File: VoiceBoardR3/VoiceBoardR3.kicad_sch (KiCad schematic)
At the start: 11 parts, among them U103 VoiceBoardConn_18P_254P, U302 TMUX4053

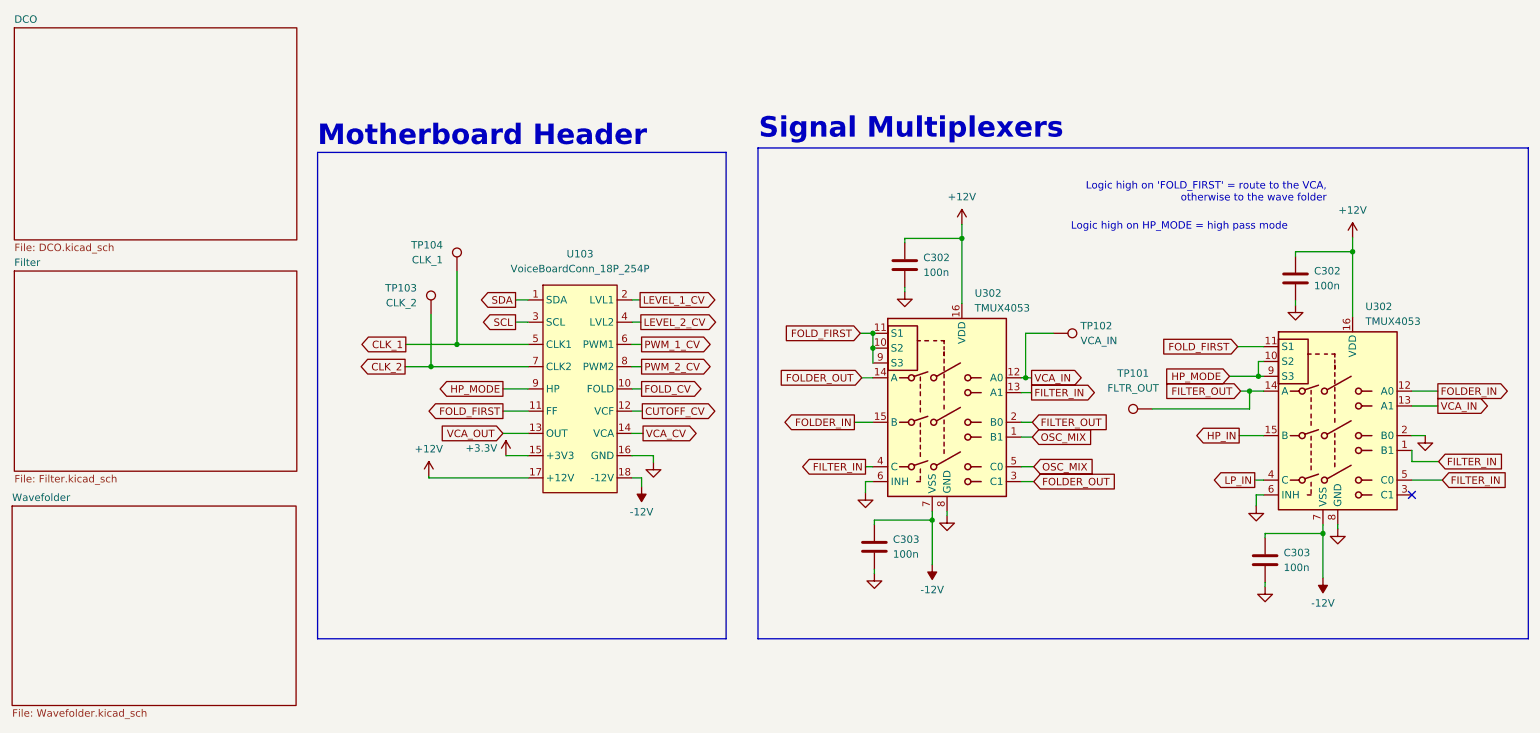
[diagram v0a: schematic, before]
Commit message: separate power supply board
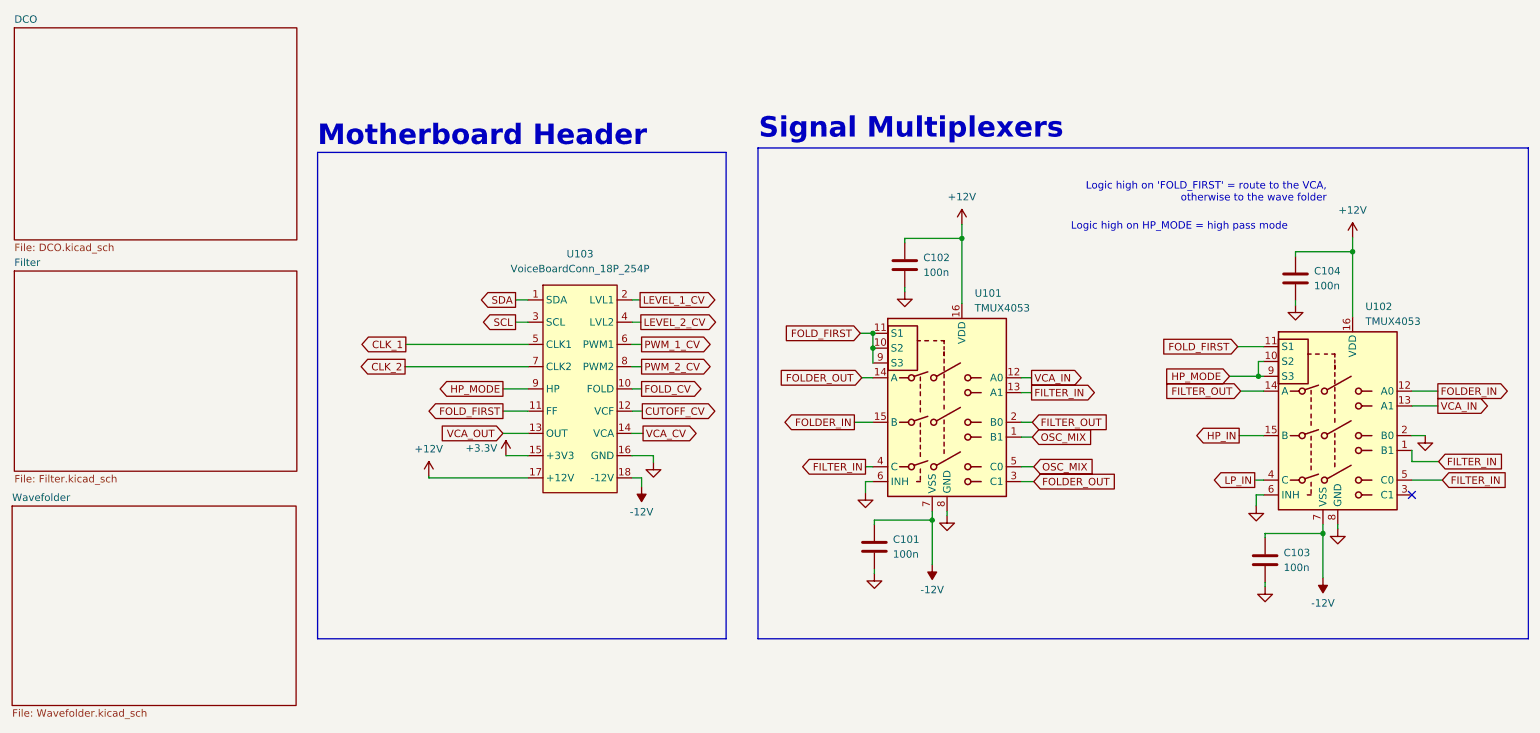
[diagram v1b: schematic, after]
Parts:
- removed TP101: FLTR_OUT, TestPoint:TestPoint_Pad_D1.0mm_Value, symbol Connector:TestPoint
- removed TP102: VCA_IN, TestPoint:TestPoint_Pad_D1.0mm_Value, symbol Connector:TestPoint
- removed TP103: CLK_2, TestPoint:TestPoint_Pad_D1.0mm_Value, symbol Connector:TestPoint
- removed TP104: CLK_1, TestPoint:TestPoint_Pad_D1.0mm_Value, symbol Connector:TestPoint
- renumbered C303 to C101, C302 to C102, C303 to C103, C302 to C104, U302 to U101, U302 to U102
